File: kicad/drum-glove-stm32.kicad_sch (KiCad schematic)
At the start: 24 parts, among them J1 SPK, J2 PZ1, J3 PZ2, J4 PZ3, SW1 SW_SPDT, U1 STM32G431KBTx, U2 PAM8302AAY

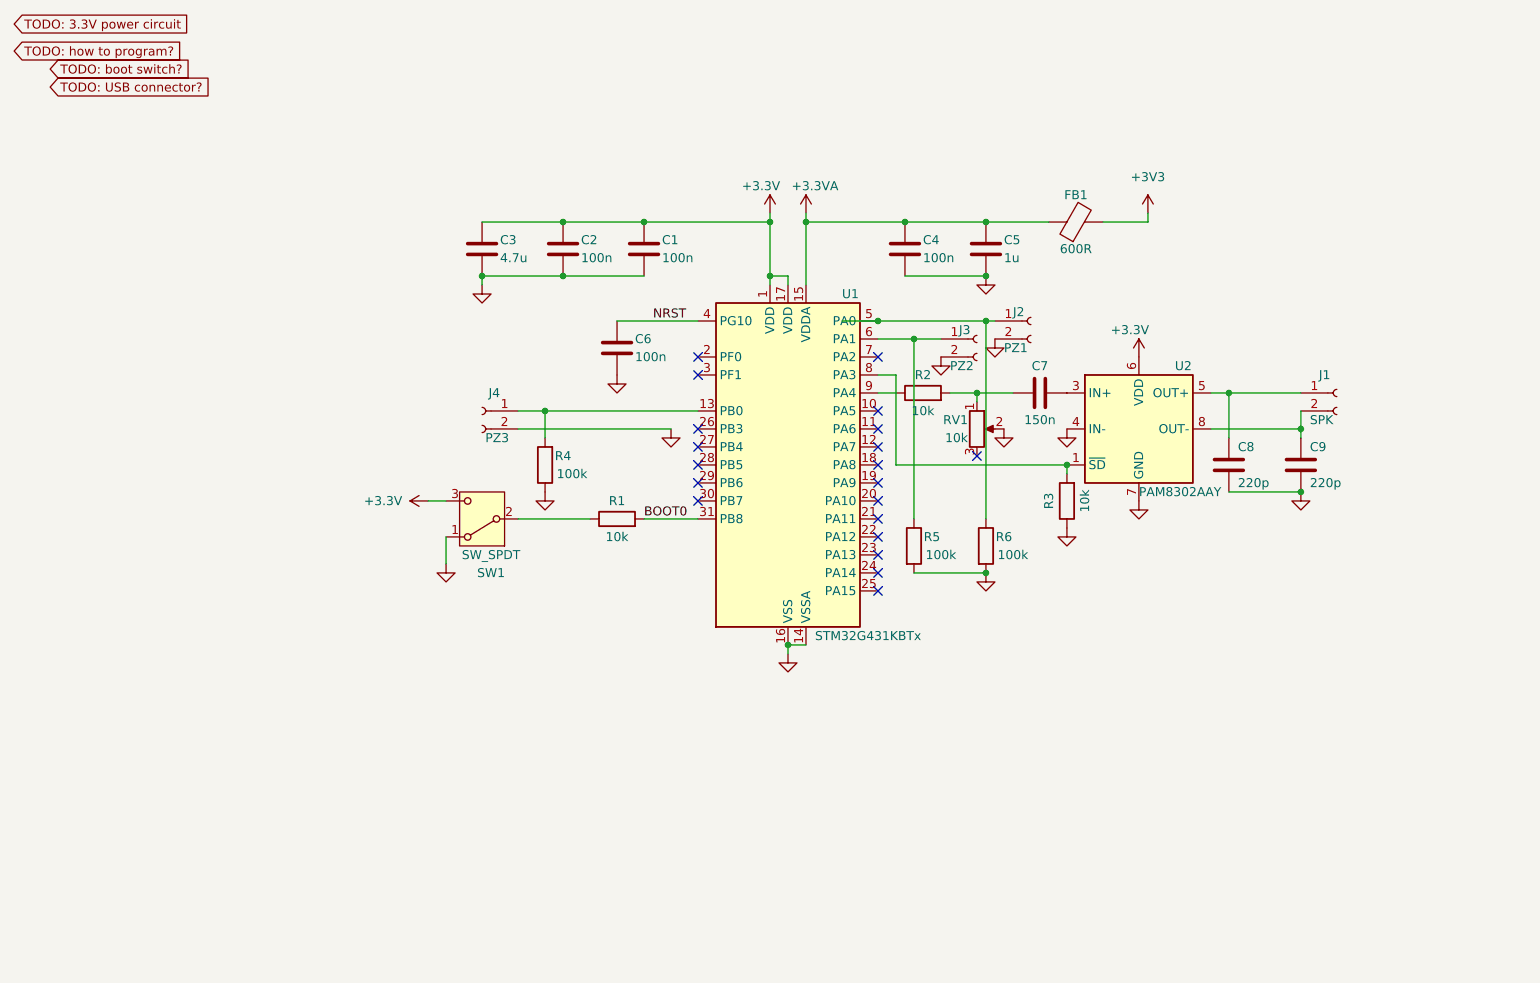
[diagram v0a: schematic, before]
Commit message: update schematic
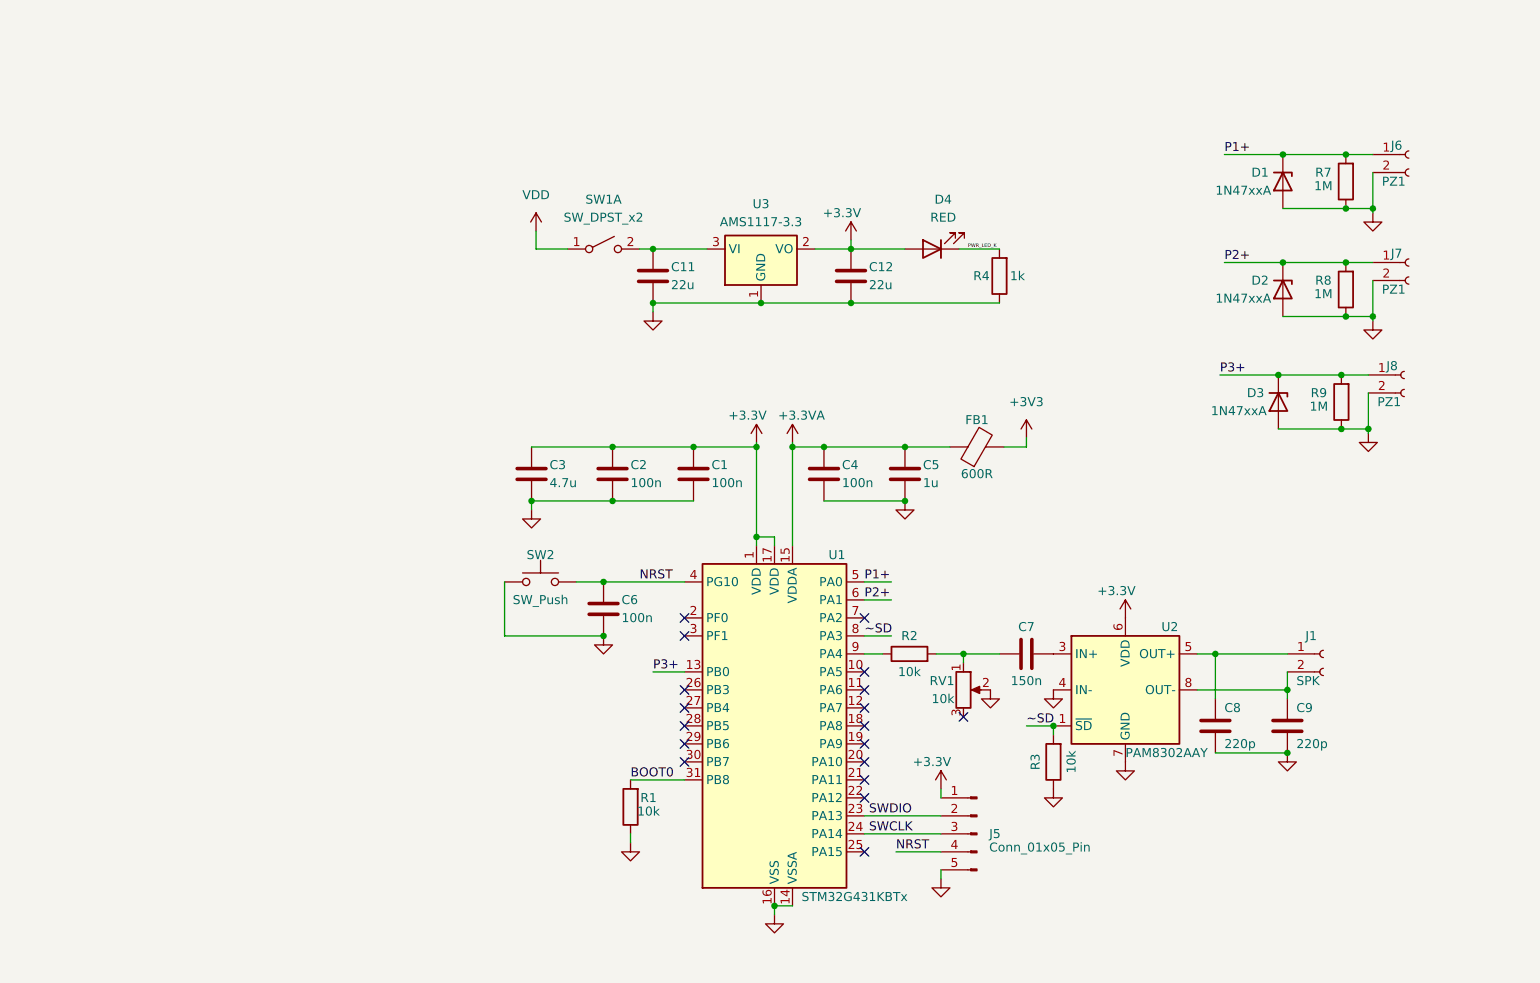
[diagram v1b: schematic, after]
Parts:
- removed J2: PZ1, symbol Connector:Conn_01x02_Socket
- removed J3: PZ2, symbol Connector:Conn_01x02_Socket
- removed J4: PZ3, symbol Connector:Conn_01x02_Socket
- removed R5, R6: 100k, symbol Device:R
- removed SW1: SW_SPDT, symbol Switch:SW_SPDT
- added C11, C12: 22u, symbol Device:C
- added D1, D2, D3: 1N47xxA, Diode_THT:D_DO-41_SOD81_P10.16mm_Horizontal, symbol Diode:1N47xxA
- added D4: RED, symbol Device:LED
- added J5: Conn_01x05_Pin, symbol Connector:Conn_01x05_Pin
- added J6, J7, J8: PZ1, symbol Connector:Conn_01x02_Socket
- added R7, R8, R9: 1M, symbol Device:R
- added SW1: SW_DPST_x2, symbol Switch:SW_DPST_x2
- added SW2: SW_Push, symbol Switch:SW_Push
- added U3: AMS1117-3.3, Package_TO_SOT_SMD:SOT-223-3_TabPin2, symbol Regulator_Linear:AMS1117-3.3
- R4: value 100k -> 1k
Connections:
- net +3.3V: now also C12.1, D4.2 (A), J5.1 (Pin_1), U3.2 (VO)
- net GND: now also R1.1, C11.2, C12.2, D1.2 (A), D2.2 (A), D3.2 (A), J5.5 (Pin_5), J6.2 (Pin_2), J7.2 (Pin_2), J8.2 (Pin_2), R7.1, R8.1, R9.1, SW2.1, U3.1 (GND)
- net NRST: now also J5.4 (Pin_4), SW2.2
- net P1+: now reaches U1.5 (PA0)
- net P1+: now also D1.1 (K), J6.1 (Pin_1), R7.2
- net P2+: now reaches U1.6 (PA1)
- net P2+: now also D2.1 (K), J7.1 (Pin_1), R8.2
- net P3+: now reaches U1.13 (PB0)
- net P3+: now also D3.1 (K), J8.1 (Pin_1), R9.2; no longer R4.2
- net ~SD: now reaches R3.2, U1.8 (PA3), U2.1 (~{SD})
- net SWDIO: now reaches U1.23 (PA13)
- net SWDIO: now also J5.2 (Pin_2)
- net SWCLK: now reaches U1.24 (PA14)
- net SWCLK: now also J5.3 (Pin_3)
- new net: C11.1, SW1.2 (B), U3.3 (VI)
- new net PWR_LED_K: D4.1 (K), R4.2
- new net VDD: SW1.1 (A)
- no-connect marks 20 -> 18
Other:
- moved on the sheet: C1, C2, C3, C4, C5, C6, C7, C8, C9, FB1, J1, R1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

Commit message: update schematic
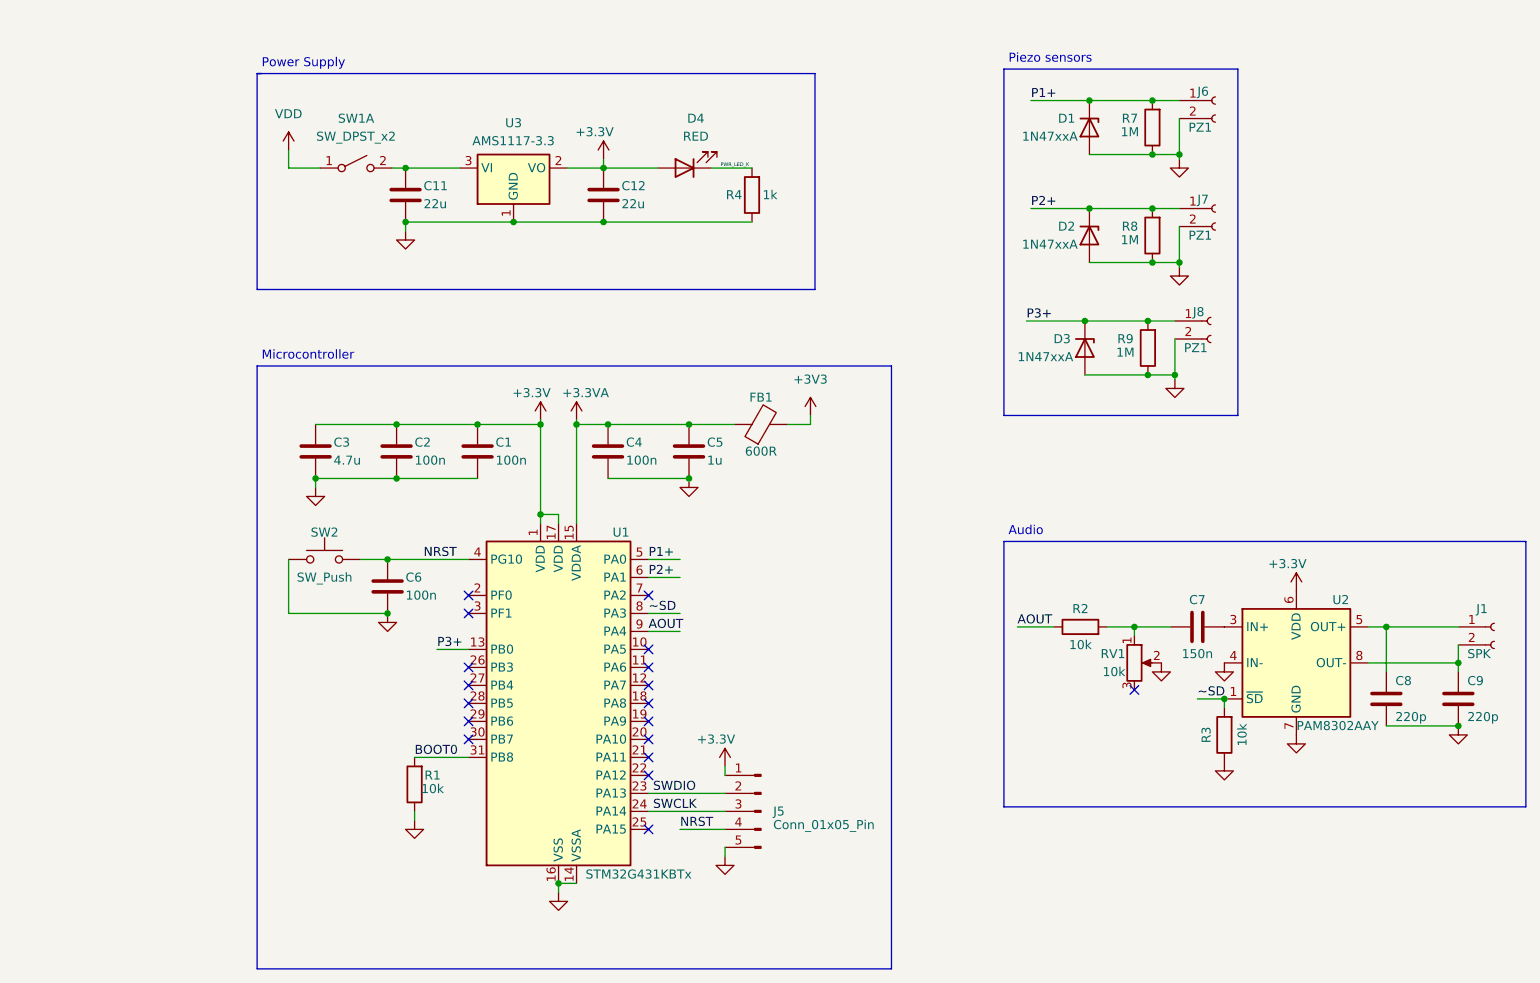
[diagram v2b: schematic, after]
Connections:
- net AOUT: now reaches R2.1, U1.9 (PA4)
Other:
- note added: "Audio"
- note added: "Microcontroller"
- note added: "Piezo sensors"
- note added: "Power Supply"
- moved on the sheet: C1, C11, C12, C2, C3, C4, C5, C6, D1, D2, D3, D4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
